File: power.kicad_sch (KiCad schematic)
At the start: 26 parts, among them SW1 GP0115ACCG30, SW2 SW_SPST, U6 BQ24072RGT, U8 NJM2884U1-33-TE1

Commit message: Release candidate
Changed USBC connector, changed TagConnect to use footprint with legs, move NRF52 to edge of board, clean up traces
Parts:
- D1, D2: MP LTST-S270TBKT -> LTST-C191TBKT
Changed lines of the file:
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@@
 			)
 		)
-		(property "Datasheet" "https://optoelectronics.liteon.com/upload/download/DS22-2000-175/LTST-S270TBKT.pdf"
+		(property "Datasheet" "https://optoelectronics.liteon.com/upload/download/DS22-2000-230/LTST-C191TBKT.pdf"
 			(at 110.49 139.7 0)
 			(effects
@@
 			)
 		)
-		(property "MP" "LTST-S270TBKT"
+		(property "MP" "LTST-C191TBKT"
 			(at 110.49 139.7 90)
 			(effects
@@
 			)
 		)
-		(property "Datasheet" "https://optoelectronics.liteon.com/upload/download/DS22-2000-175/LTST-S270TBKT.pdf"
+		(property "Datasheet" "https://optoelectronics.liteon.com/upload/download/DS22-2000-230/LTST-C191TBKT.pdf"
 			(at 99.06 139.7 0)
 			(effects
@@
 			)
 		)
-		(property "MP" "LTST-S270TBKT"
+		(property "MP" "LTST-C191TBKT"
 			(at 99.06 139.7 90)
 			(effects

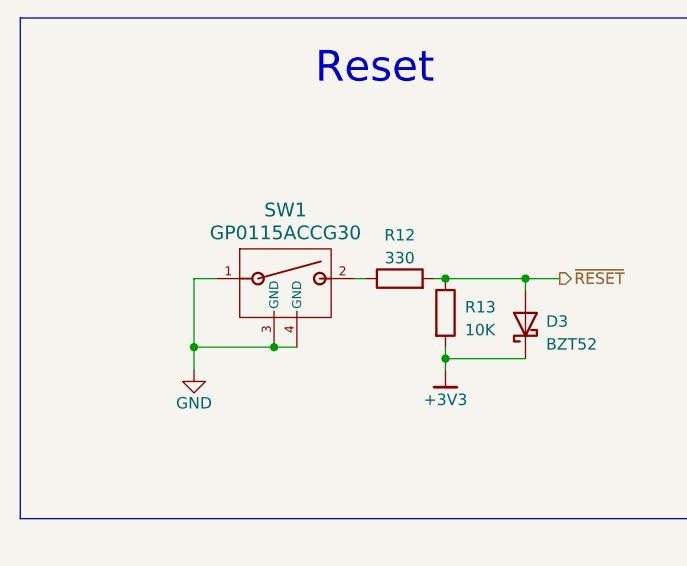
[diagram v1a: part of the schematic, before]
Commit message: Changed reset button, upgrade to new KiCad
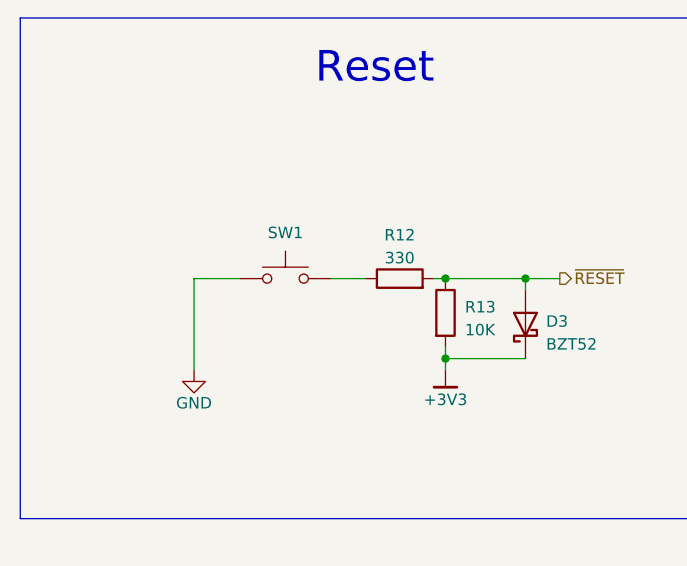
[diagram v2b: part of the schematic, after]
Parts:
- removed SW1: GP0115ACCG30, GP0115ACCG30:SW_GP0115ACCG30_NKK, symbol GP0115ACCG30:GP0115ACCG30
- added SW1: (no value), Button_Switch_THT:SW_SPST_Omron_B3F-315x_Angled, symbol Switch:SW_Push
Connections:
- net GND: now also SW1.1
- net at R12.1: now also SW1.2
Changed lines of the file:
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@@
-	)
-	(junction
-		(at 39.37 54.61)
-		(diameter 0)
-		(color 0 0 0 0)
 	)
 	(junction
@@
 	)
 	(junction
-		(at 48.26 54.61)
-		(diameter 0)
-		(color 0 0 0 0)
-	)
-	(junction
 		(at 128.27 146.05)
 		(diameter 0)
@@
 	(wire
 		(pts
-			(xy 57.15 46.99) (xy 58.42 46.99)
-		)
-		(stroke
-			(width 0)
-			(type default)
-		)
-	)
-	(wire
-		(pts
 			(xy 177.8 119.38) (xy 177.8 120.65)
 		)
@@
 	(wire
 		(pts
-			(xy 39.37 46.99) (xy 41.91 46.99)
+			(xy 39.37 46.99) (xy 44.45 46.99)
 		)
 		(stroke
@@
 	(wire
 		(pts
-			(xy 39.37 54.61) (xy 48.26 54.61)
-		)
-		(stroke
-			(width 0)
-			(type default)
-		)
-	)
-	(wire
-		(pts
 			(xy 184.15 119.38) (xy 177.8 119.38)
 		)
@@
 	(wire
 		(pts
-			(xy 48.26 54.61) (xy 50.8 54.61)
-		)
-		(stroke
-			(width 0)
-			(type default)
-		)
-	)
-	(wire
-		(pts
 			(xy 100.33 116.84) (xy 102.87 116.84)
 		)
@@
 	(wire
 		(pts
-			(xy 39.37 46.99) (xy 39.37 54.61)
+			(xy 39.37 46.99) (xy 39.37 57.15)
 		)
 		(stroke
@@
 	(wire
 		(pts
+			(xy 54.61 46.99) (xy 58.42 46.99)
+		)
+		(stroke
+			(width 0)
+			(type default)
+		)
+	)
+	(wire
+		(pts
 			(xy 120.65 146.05) (xy 128.27 146.05)
 		)
@@
 		(pts
 			(xy 149.86 115.57) (xy 149.86 116.84)
-		)
-		(stroke
-			(width 0)
-			(type default)
-		)
-	)
-	(wire
-		(pts
-			(xy 39.37 54.61) (xy 39.37 57.15)
 		)
 		(stroke
@@
 			)
 			(justify left)
+		)
+	)
+	(symbol
+		(lib_id "Switch:SW_Push")
+		(at 49.53 46.99 0)
+		(unit 1)
+		(exclude_from_sim no)
+		(in_bom yes)
+		(on_board yes)
+		(dnp no)
+		(fields_autoplaced yes)
+		(property "Reference" "SW1"
+			(at 49.53 41.91 0)
+			(effects
+				(font
+					(size 1.27 1.27)
+				)
+			)
+		)
+		(property "Value" ""
+			(at 49.53 41.91 0)
+			(effects
+				(font
+					(size 1.27 1.27)
+				)
+			)
+		)
+		(property "Footprint" "Button_Switch_THT:SW_SPST_Omron_B3F-315x_Angled"
+			(at 49.53 41.91 0)
+			(effects
+				(font
+					(size 1.27 1.27)
+				)
+				(hide yes)
+			)
+		)
+		(property "Datasheet" "~"
+			(at 49.53 41.91 0)
+			(effects
+				(font
+					(size 1.27 1.27)
+				)
+				(hide yes)
+			)
+		)
+		(property "Description" "Push button switch, generic, two pins"
+			(at 49.53 46.99 0)
+			(effects
+				(font
+					(size 1.27 1.27)
+				)
+				(hide yes)
+			)
+		)
+		(pin "2"
+		)
+		(pin "1"
+		)
+		(instances
+			(project ""
+				(path "/000b185d-3cb3-4b02-ba95-82af8e0bb160/d2aaa24e-aace-4a2d-94e1-427822a5d83f"
+					(reference "SW1")
+					(unit 1)
+				)
+			)
 		)
 	)
@@
 	)
 	(symbol
-		(lib_id "GP0115ACCG30:GP0115ACCG30")
-		(at 41.91 46.99 0)
-		(unit 1)
-		(exclude_from_sim no)
-		(in_bom yes)
-		(on_board yes)
-		(dnp no)
-		(fields_autoplaced yes)
-		(property "Reference" "SW1"
-			(at 49.53 39.37 0)
-			(effects
-				(font
-					(size 1.524 1.524)
-				)
-			)
-		)
-		(property "Value" "GP0115ACCG30"
-			(at 49.53 41.91 0)
-			(effects
-				(font
-					(size 1.524 1.524)
-				)
-			)
-		)
-		(property "Footprint" "GP0115ACCG30:SW_GP0115ACCG30_NKK"
-			(at 41.91 40.005 0)
-			(effects
-				(font
-					(size 1.27 1.27)
-					(italic yes)
-				)
-				(hide yes)
-			)
-		)
-		(property "Datasheet" "https://www.nkkswitches.com/pdf/GP01.pdf"
-			(at 41.91 40.005 0)
-			(effects
-				(font
-					(size 1.27 1.27)
-					(italic yes)
-				)
-				(hide yes)
-			)
-		)
-		(property "Description" ""
-			(at 41.91 46.99 0)
-			(effects
-				(font
-					(size 1.27 1.27)
-				)
-				(hide yes)
-			)
-		)
-		(property "MP" "GP0115ACCG30"
-			(at 41.91 46.99 0)
-			(effects
-				(font
-					(size 1.27 1.27)
-				)
-				(hide yes)
-			)
-		)
-		(property "Alt" ""
-			(at 41.91 46.99 0)
-			(effects
-				(font
-					(size 1.27 1.27)
-				)
-			)
-		)
-		(property "MAXIMUM_PACKAGE_HIEGHT" ""
-			(at 41.91 46.99 0)
-			(effects
-				(font
-					(size 1.27 1.27)
-				)
-			)
-		)
-		(property "MPN" ""
-			(at 41.91 46.99 0)
-			(effects
-				(font
-					(size 1.27 1.27)
-				)
-			)
-		)
-		(pin "2"
-		)
-		(pin "4"
-		)
-		(pin "1"
-		)
-		(pin "3"
-		)
-		(instances
-			(project ""
-				(path "/000b185d-3cb3-4b02-ba95-82af8e0bb160/d2aaa24e-aace-4a2d-94e1-427822a5d83f"
-					(reference "SW1")
-					(unit 1)
-				)
-			)
-		)
-	)
-	(symbol
 		(lib_id "Device:R")
 		(at 110.49 149.86 180)
@@
 			)
 		)
-		(property "Datasheet" "https://datasheets.kyocera-avx.com/tc-series.pdf"
+		(property "Datasheet" "~"
 			(at 231.14 125.73 0)
 			(effects
@@
 			)
 		)
-		(property "Description" ""
+		(property "Description" "Polarized capacitor"
 			(at 231.14 125.73 0)
 			(effects

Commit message: Added MP part number fields to schematic and PCB design,
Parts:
- SW1: value (none) -> ~; MP (none) -> B3F-3155
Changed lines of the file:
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@@
 			)
 		)
-		(property "Value" ""
+		(property "Value" "~"
 			(at 49.53 41.91 0)
 			(effects
@@
 			(at 49.53 46.99 0)
 			(effects
+				(font
+					(size 1.27 1.27)
+				)
+				(hide yes)
+			)
+		)
+		(property "MP" "B3F-3155"
+			(at 49.53 46.99 0)
+			(effects
